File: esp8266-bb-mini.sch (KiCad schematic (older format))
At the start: 25 parts, among them J1 Conn_01x04_Male, J2 Conn_01x04_Male, J3 Conn_01x04_Male, J4 Conn_01x04_Male, J5 Conn_01x02_Male, U1 LP38693MP-3.3, U2 ESP-12F

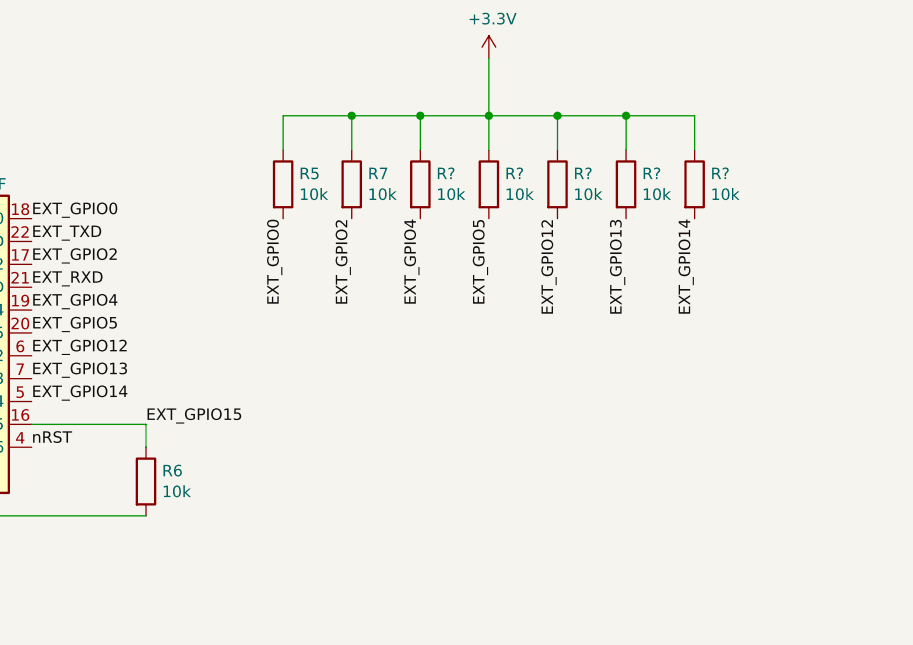
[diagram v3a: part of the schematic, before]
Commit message: new layout with bigger connectors
Signed-off-by: Tillmann Heidsieck <theidsieck@leenox.de>
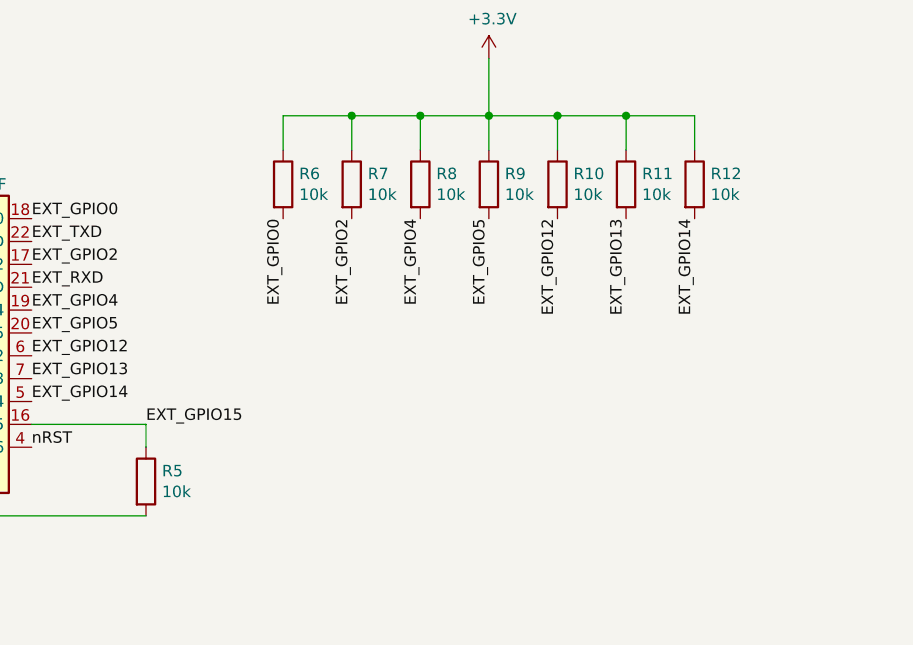
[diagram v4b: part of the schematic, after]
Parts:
- J1, J2, J3, J4: footprint Connector_Molex:Molex_PicoBlade_53048-0410_1x04_P1.25mm_Horizontal -> Connector_JST:JST_XH_B4B-XH-A_1x04_P2.50mm_Vertical
- J5: footprint Connector_Molex:Molex_PicoBlade_53048-0210_1x02_P1.25mm_Horizontal -> Connector_JST:JST_XH_B2B-XH-A_1x02_P2.50mm_Vertical
- gave numbers to parts that had none: 5
- renumbered R6 to R5, R5 to R6
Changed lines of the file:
@@
 F 0 "J5" H 8608 2331 50  0000 C CNN
 F 1 "Conn_01x02_Male" H 8608 2240 50  0000 C CNN
-F 2 "Connector_Molex:Molex_PicoBlade_53048-0210_1x02_P1.25mm_Horizontal" H 8500 2150 50  0001 C CNN
+F 2 "Connector_JST:JST_XH_B2B-XH-A_1x02_P2.50mm_Vertical" H 8500 2150 50  0001 C CNN
 F 3 "~" H 8500 2150 50  0001 C CNN
 	1    8500 2150
@@
 F 0 "J1" H 6708 1681 50  0000 C CNN
 F 1 "Conn_01x04_Male" H 6708 1590 50  0000 C CNN
-F 2 "Connector_Molex:Molex_PicoBlade_53048-0410_1x04_P1.25mm_Horizontal" H 6600 1400 50  0001 C CNN
+F 2 "Connector_JST:JST_XH_B4B-XH-A_1x04_P2.50mm_Vertical" H 6600 1400 50  0001 C CNN
 F 3 "~" H 6600 1400 50  0001 C CNN
 	1    6600 1400
@@
 F 0 "J3" H 6708 3131 50  0000 C CNN
 F 1 "Conn_01x04_Male" H 6708 3040 50  0000 C CNN
-F 2 "Connector_Molex:Molex_PicoBlade_53048-0410_1x04_P1.25mm_Horizontal" H 6600 2850 50  0001 C CNN
+F 2 "Connector_JST:JST_XH_B4B-XH-A_1x04_P2.50mm_Vertical" H 6600 2850 50  0001 C CNN
 F 3 "~" H 6600 2850 50  0001 C CNN
 	1    6600 2850
@@
 $EndComp
 $Comp
-L Device:R R6
+L Device:R R5
 U 1 1 5FB5E914
 P 5600 5600
-F 0 "R6" H 5670 5646 50  0000 L CNN
+F 0 "R5" H 5670 5646 50  0000 L CNN
 F 1 "10k" H 5670 5555 50  0000 L CNN
 F 2 "Resistor_SMD:R_0402_1005Metric" V 5530 5600 50  0001 C CNN
@@
 $EndComp
 $Comp
-L Device:R R5
+L Device:R R6
 U 1 1 5FB599F1
 P 6200 4300
-F 0 "R5" H 6270 4346 50  0000 L CNN
+F 0 "R6" H 6270 4346 50  0000 L CNN
 F 1 "10k" H 6270 4255 50  0000 L CNN
 F 2 "Resistor_SMD:R_0402_1005Metric" V 6130 4300 50  0001 C CNN
@@
 F 0 "J4" H 8608 1631 50  0000 C CNN
 F 1 "Conn_01x04_Male" H 8608 1540 50  0000 C CNN
-F 2 "Connector_Molex:Molex_PicoBlade_53048-0410_1x04_P1.25mm_Horizontal" H 8500 1350 50  0001 C CNN
+F 2 "Connector_JST:JST_XH_B4B-XH-A_1x04_P2.50mm_Vertical" H 8500 1350 50  0001 C CNN
 F 3 "~" H 8500 1350 50  0001 C CNN
 	1    8500 1350
@@
 F 0 "J2" H 6708 2381 50  0000 C CNN
 F 1 "Conn_01x04_Male" H 6708 2290 50  0000 C CNN
-F 2 "Connector_Molex:Molex_PicoBlade_53048-0410_1x04_P1.25mm_Horizontal" H 6600 2100 50  0001 C CNN
+F 2 "Connector_JST:JST_XH_B4B-XH-A_1x04_P2.50mm_Vertical" H 6600 2100 50  0001 C CNN
 F 3 "~" H 6600 2100 50  0001 C CNN
 	1    6600 2100
@@
 $EndComp
 $Comp
-L power:+BATT #PWR016
+L power:+BATT #PWR017
 U 1 1 5FBF99E2
 P 8700 2150
-F 0 "#PWR016" H 8700 2000 50  0001 C CNN
+F 0 "#PWR017" H 8700 2000 50  0001 C CNN
 F 1 "+BATT" H 8715 2323 50  0000 C CNN
 F 2 "" H 8700 2150 50  0001 C CNN
@@
 $EndComp
 $Comp
-L power:-BATT #PWR017
+L power:-BATT #PWR018
 U 1 1 5FBFD1FA
 P 8700 2250
-F 0 "#PWR017" H 8700 2100 50  0001 C CNN
+F 0 "#PWR018" H 8700 2100 50  0001 C CNN
 F 1 "-BATT" H 8715 2423 50  0000 C CNN
 F 2 "" H 8700 2250 50  0001 C CNN
@@
 EXT_GPIO12
 $Comp
-L Device:R R?
+L Device:R R8
 U 1 1 5FED4C62
 P 6800 4300
-F 0 "R?" H 6870 4346 50  0000 L CNN
+F 0 "R8" H 6870 4346 50  0000 L CNN
 F 1 "10k" H 6870 4255 50  0000 L CNN
 F 2 "Resistor_SMD:R_0402_1005Metric" V 6730 4300 50  0001 C CNN
@@
 $EndComp
 $Comp
-L Device:R R?
+L Device:R R9
 U 1 1 5FED53C5
 P 7100 4300
-F 0 "R?" H 7170 4346 50  0000 L CNN
+F 0 "R9" H 7170 4346 50  0000 L CNN
 F 1 "10k" H 7170 4255 50  0000 L CNN
 F 2 "Resistor_SMD:R_0402_1005Metric" V 7030 4300 50  0001 C CNN
@@
 $EndComp
 $Comp
-L Device:R R?
+L Device:R R10
 U 1 1 5FED6300
 P 7400 4300
-F 0 "R?" H 7470 4346 50  0000 L CNN
+F 0 "R10" H 7470 4346 50  0000 L CNN
 F 1 "10k" H 7470 4255 50  0000 L CNN
 F 2 "Resistor_SMD:R_0402_1005Metric" V 7330 4300 50  0001 C CNN
@@
 $EndComp
 $Comp
-L Device:R R?
+L Device:R R11
 U 1 1 5FED6B2D
 P 7700 4300
-F 0 "R?" H 7770 4346 50  0000 L CNN
+F 0 "R11" H 7770 4346 50  0000 L CNN
 F 1 "10k" H 7770 4255 50  0000 L CNN
 F 2 "Resistor_SMD:R_0402_1005Metric" V 7630 4300 50  0001 C CNN
@@
 $EndComp
 $Comp
-L Device:R R?
+L Device:R R12
 U 1 1 5FED7182
 P 8000 4300
-F 0 "R?" H 8070 4346 50  0000 L CNN
+F 0 "R12" H 8070 4346 50  0000 L CNN
 F 1 "10k" H 8070 4255 50  0000 L CNN
 F 2 "Resistor_SMD:R_0402_1005Metric" V 7930 4300 50  0001 C CNN
@@
 	7100 4000 7100 3750
 $Comp
-L power:+3.3V #PWR?
+L power:+3.3V #PWR016
 U 1 1 5FEDEC55
 P 7100 3750
-F 0 "#PWR?" H 7100 3600 50  0001 C CNN
+F 0 "#PWR016" H 7100 3600 50  0001 C CNN
 F 1 "+3.3V" H 7115 3923 50  0000 C CNN
 F 2 "" H 7100 3750 50  0001 C CNN
